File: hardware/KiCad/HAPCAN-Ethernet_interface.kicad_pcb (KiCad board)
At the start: 2 copper layers, 86.5 x 33 mm, 84 parts, among them CON1 Connectors CAN bus, IC1 LMR51430Y, IC2 MCP2561-E-SN, IC3 TLV62568DRL, IC4 STM32F072C8Tx, IC5 MCP3422A0-E/MS, IC6 USBLC6-2SC6, IC7 FT230XS, U1 HLK-7628N

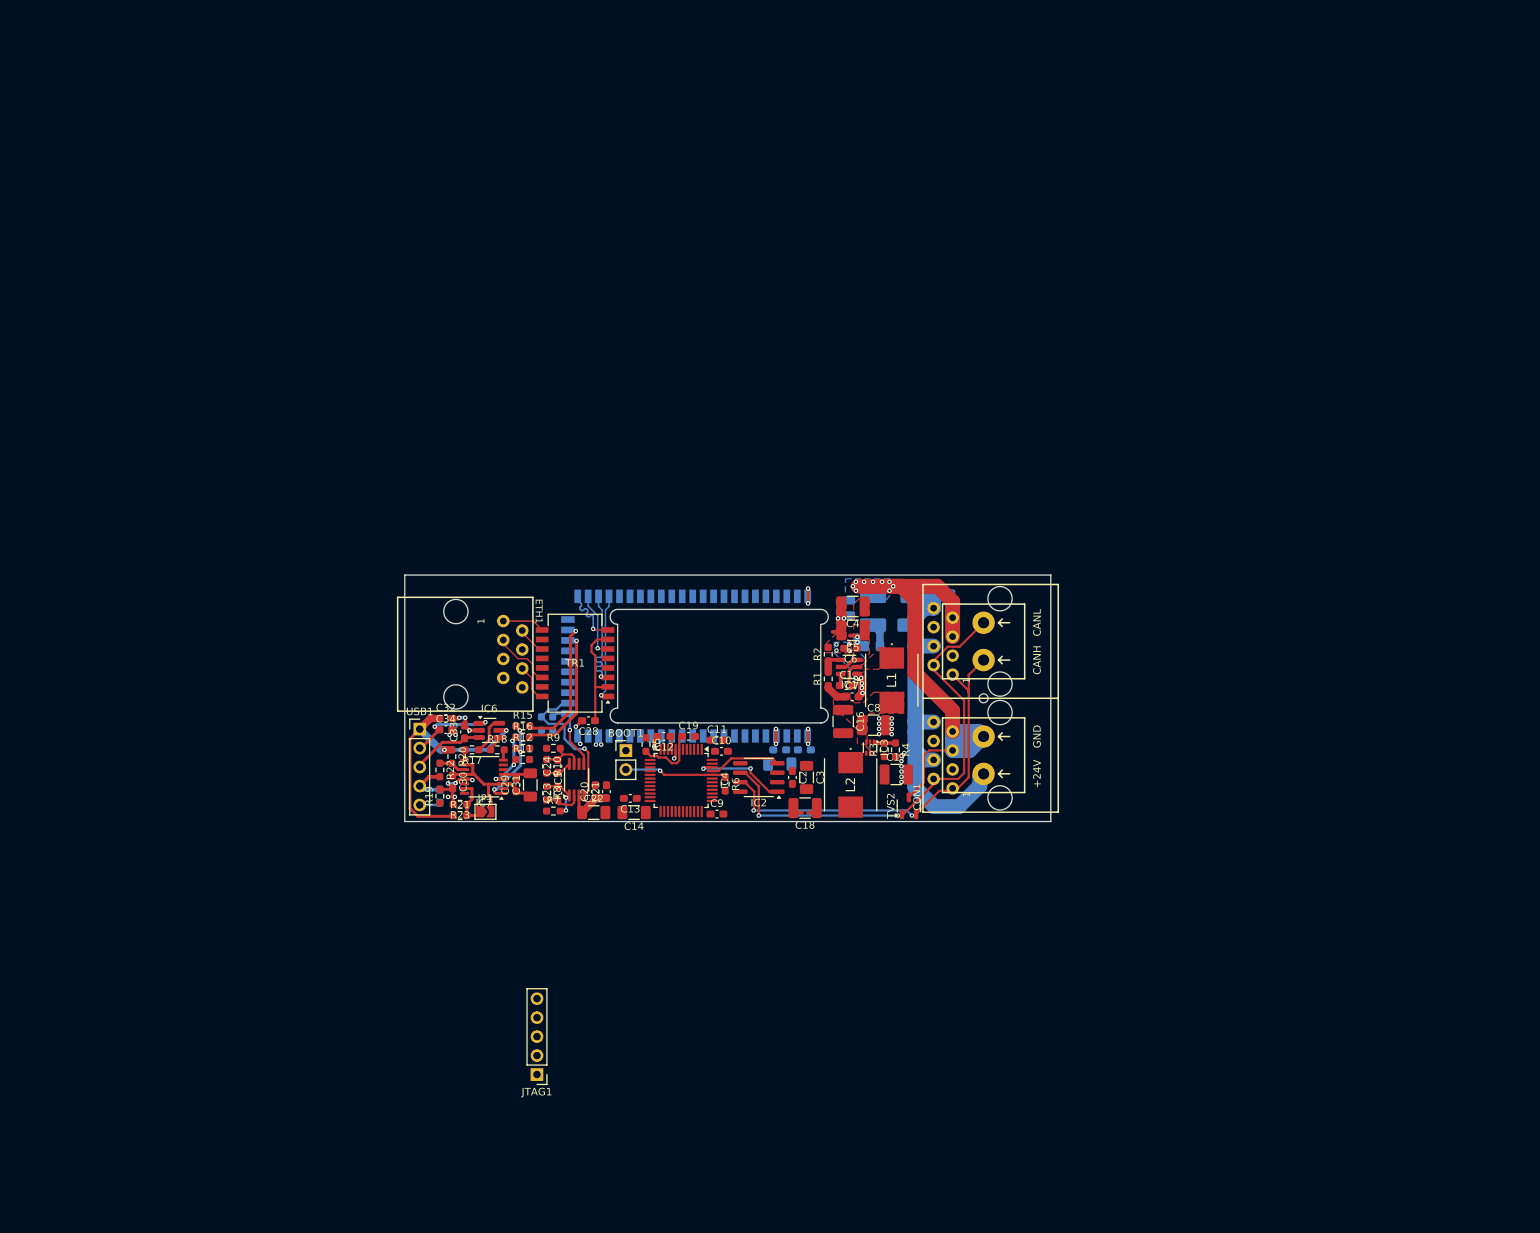
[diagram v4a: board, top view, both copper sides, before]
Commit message: Updated schematic, finished the board routing
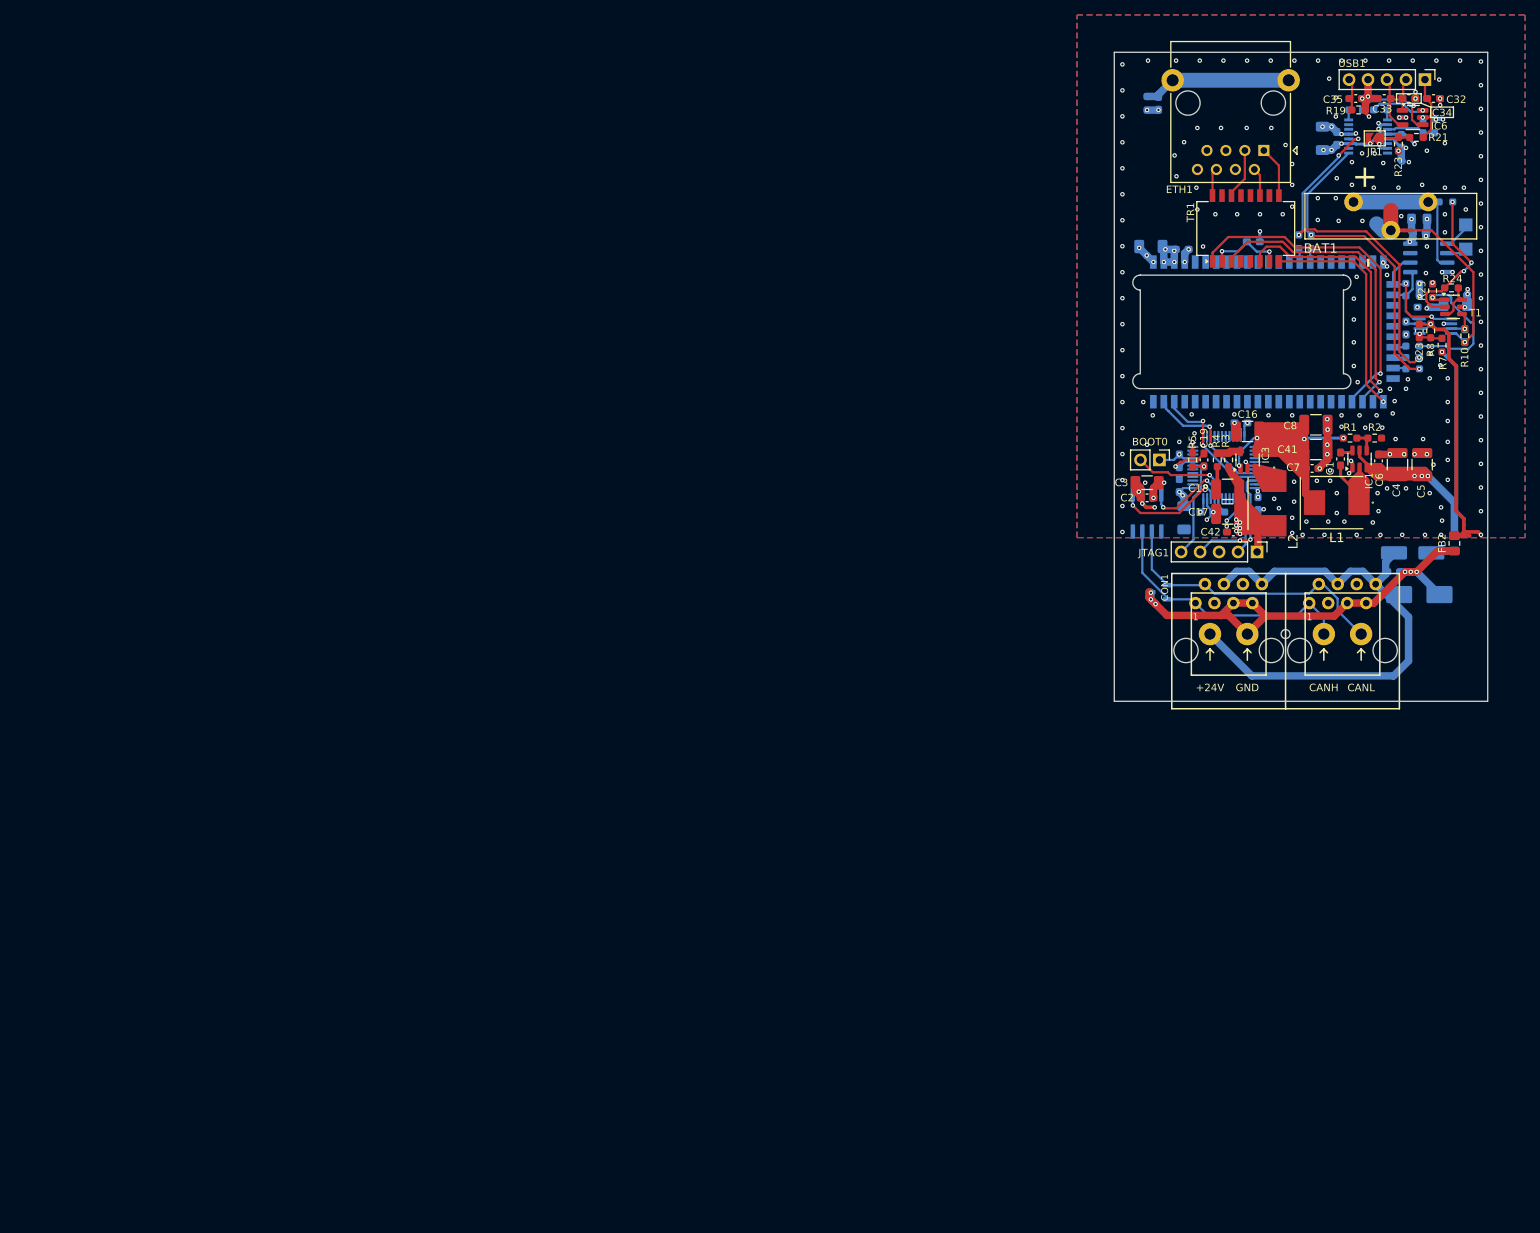
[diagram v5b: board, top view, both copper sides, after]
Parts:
- removed BOOT1: Jumper_2_Open, Connector_PinHeader_2.54mm:PinHeader_1x02_P2.54mm_Vertical
- removed C26: 100n, Capacitor_SMD:C_0603_1608Metric_Pad1.08x0.95mm_HandSolder
- removed NT3: NetTie_2, NetTie:NetTie-2_SMD_Pad0.5mm
- added BAT1: CR2032, ProjectLib:1074, F.Cu at (227.0, 50.0)
- added BOOT0: Jumper_2_Open, Connector_PinHeader_2.54mm:PinHeader_1x02_P2.54mm_Vertical, F.Cu at (201.0, 84.6)
- added C36: 1u, Capacitor_SMD:C_0805_2012Metric_Pad1.18x1.45mm_HandSolder, B.Cu at (235.8, 52.3)
- added C37: 100n, Capacitor_SMD:C_0603_1608Metric_Pad1.08x0.95mm_HandSolder, B.Cu at (235.8, 54.1)
- added C38: 330p, Capacitor_SMD:C_0603_1608Metric_Pad1.08x0.95mm_HandSolder, B.Cu at (200.9, 36.8)
- added C41: 10u 16V, Capacitor_SMD:C_1210_3225Metric_Pad1.33x2.70mm_HandSolder, F.Cu at (222.0, 83.2)
- added C42: 100n, Capacitor_SMD:C_0603_1608Metric_Pad1.08x0.95mm_HandSolder, F.Cu at (210.9, 94.2)
- added IC8: BQ32000, Package_SO:SOIC-8_3.9x4.9mm_P1.27mm, B.Cu at (237.1, 57.5)
- added R24: 47k, Resistor_SMD:R_0603_1608Metric_Pad0.98x0.95mm_HandSolder, F.Cu at (240.2, 61.5)
- added R25: 47k, Resistor_SMD:R_0603_1608Metric_Pad0.98x0.95mm_HandSolder, F.Cu at (237.6, 61.9)
- added R26: 330R, Resistor_SMD:R_0603_1608Metric_Pad0.98x0.95mm_HandSolder, B.Cu at (234.9, 69.3)
- added R27: 1M, Resistor_SMD:R_0603_1608Metric_Pad0.98x0.95mm_HandSolder, B.Cu at (199.4, 36.8)
- added T1: DMC2053UVT, Package_TO_SOT_SMD:TSOT-23-6, F.Cu at (240.4, 64.1)
- added XTAL1: ECS-.327-12.5-34QCS-TR, Crystal:Crystal_SMD_EuroQuartz_EQ161-2Pin_3.2x1.5mm_HandSoldering, B.Cu at (242.1, 54.7)
- C10, C11, C12, C13, C14, C20, C21, C22, C24, C28, C29, C30, C31, C9, IC2, IC4, IC5, IC7, NT1, R11, R12, R15, R16, R17, R18, R20, R22, R6, R9, TVS2: moved to B.Cu
- C35, FB2: moved to F.Cu
- ETH1: value RJ45 -> RJ45_Shielded; footprint ProjectLib:RJ45-PCB-SOCKET -> Connector_RJ:RJ45_Ninigi_GE
- IC3: value TLV62568DRL -> TLV62568DBV; footprint Package_TO_SOT_SMD:SOT-563 -> Package_TO_SOT_SMD:SOT-23-5
- R13, R14: value 10k -> 4k7
- moved USB1 160.2 mm to (236.6, 33.7), turned to -90 degrees
- moved R22 158.6 mm to (237.9, 39.9), turned to 90 degrees
- moved R21 157.0 mm to (235.5, 41.4), turned to 180 degrees
- moved C32 156.1 mm to (237.7, 36.2)
- moved R20 155.0 mm to (236.3, 39.9)
- moved C34 154.2 mm to (234.4, 36.2)
- moved C35 154.2 mm to (227.3, 36.2), turned to 0 degrees
- moved R23 153.6 mm to (233.0, 42.3), turned to -90 degrees
- moved R19 153.5 mm to (227.7, 37.7), turned to 0 degrees
- moved C30 153.3 mm to (233.4, 41.9)
- moved C33 149.5 mm to (231.1, 36.2), turned to 180 degrees
- moved JP1 149.4 mm to (229.9, 41.5), turned to 180 degrees
- moved R17 148.8 mm to (230.6, 37.7), turned to 0 degrees
- moved IC6 148.4 mm to (234.9, 38.7)
- moved IC7 146.2 mm to (229.0, 41.3), turned to 0 degrees
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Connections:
- IC3 pad 1: Net-(IC3-FB) -> +5V
- IC3 pad 3: +5V -> Net-(IC3-SW)
- IC3 pad 4: Net-(IC3-SW) -> +5V
- IC3 pad 5: +5V -> Net-(IC3-FB)
- R9 pad 1: /ADC_3V3 -> /ADC_BAT
- R9 pad 2: Net-(IC5-CH2+) -> +BATT
- U1 pad 30: unconnected-(U1-GPIO0-Pad30) -> /BAT_MEAS_EN
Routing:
- net GND: track 48.3 -> 98.6 mm, vias 47 -> 231
- net +5V: track 4.85 -> 48.0 mm, vias 0 -> 6
- net /UART_FTDI_Rx: track 8.85 -> 48.7 mm, vias 3 -> 4
- net /PHY_TX-: track 15.0 -> 46.0 mm
- net /UART_FTDI_Tx: track 12.7 -> 42.2 mm, vias 3 -> 2
- net +3V3: track 26.5 -> 55.4 mm, vias 0 -> 31
- net /PHY_TX+: track 13.6 -> 41.1 mm
- net /ADC_GND: track 5.38 -> 32.6 mm, vias 0 -> 1
- net /PHY_RX-: track 8.89 -> 36.0 mm
- net VBUS: track 36.4 -> 10.2 mm, vias 2 -> 1
- net /CANL: track 62.9 -> 38.8 mm, vias 2 -> 0
- net /PHY_RX+: track 8.90 -> 30.4 mm
- net /ADC_BAT: track 0.00 -> 20.8 mm, vias 0 -> 3
- net Net-(C38-Pad1): track 0.00 -> 20.1 mm
- net /CANH: track 55.9 -> 36.0 mm, vias 2 -> 0
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- added copper zone on In2.Cu, net +3V3
- added copper zone on In1.Cu, net GND
- removed copper zone on F.Cu, net +24V
- removed copper zone on F.Cu, net +5V
- removed copper zone on B.Cu, net GNDPWR
- removed copper zone on F.Cu, net Net-(IC1-SW)
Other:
- board size 86.5 x 33 mm -> 50 x 86.9 mm
- copper layers 2 -> 4

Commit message: Finished the board (Rev. 0)
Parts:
- moved FB2 2.41 mm to (240.5, 98.2)
- moved NT2 2.04 mm to (241.7, 95.8)
- moved R9 1.14 mm to (240.5, 50.0)
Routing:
- net GND: track 98.6 -> 109.6 mm, vias 231 -> 254
- net +BATT: track 19.3 -> 22.4 mm
- net /ADC_GND: track 32.6 -> 34.6 mm
- net GNDPWR: track 64.9 -> 63.9 mm
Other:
- board text added: "Designed by Ondřej Kolář"
- board text added: "HAPCAN Linux module"
- board text added: "Rev. 0 ${CURRENT_DATE}"

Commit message: Fixed a resistor value near the ADC, added some notes to the schematic
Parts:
- R24: value 47k -> 1M
